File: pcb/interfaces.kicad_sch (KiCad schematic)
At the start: 6 parts

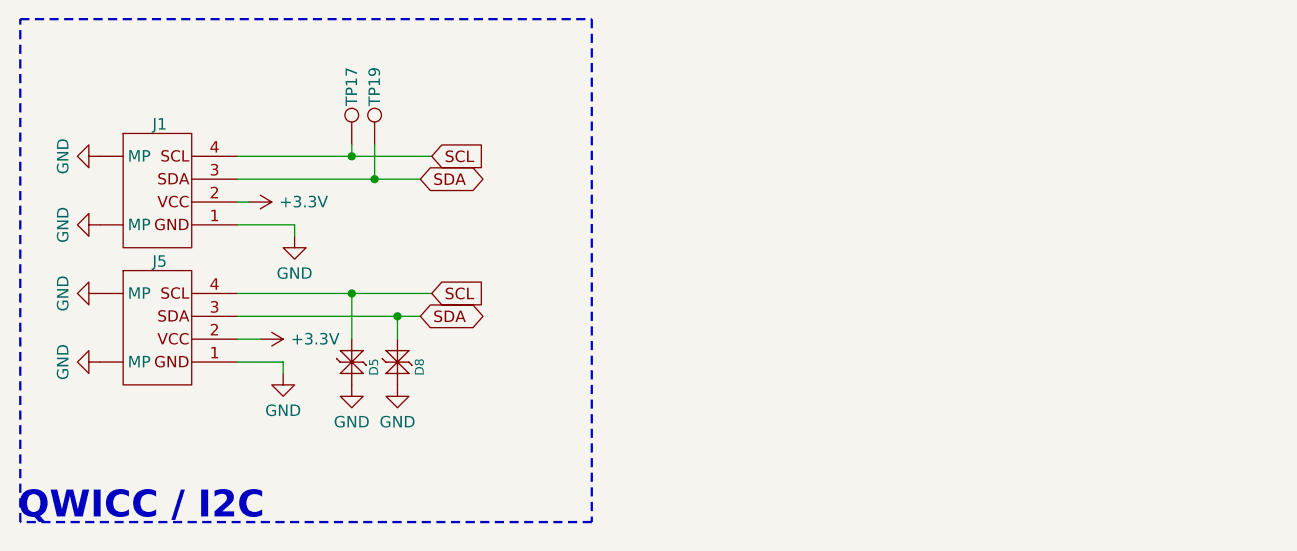
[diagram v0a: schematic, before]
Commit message: refactored to STM32
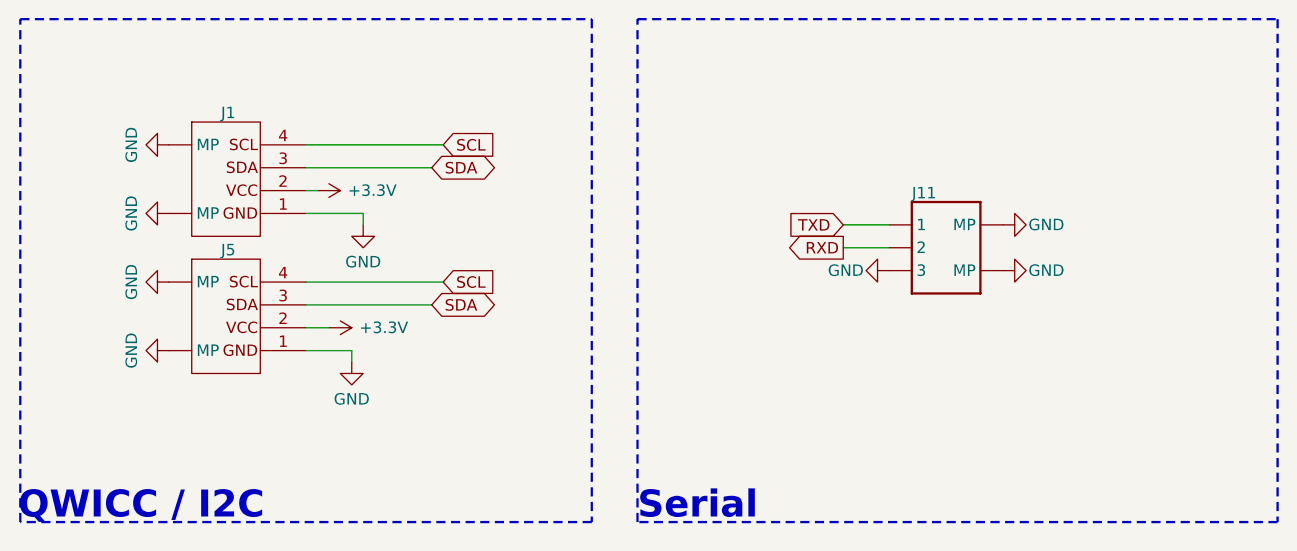
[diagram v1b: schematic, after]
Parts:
- removed D5, D8: PESD3V3S1BL, CRGM Passive:DFN1006-2, symbol CRGM Passive:PESD3V3S1BL
- removed TP17, TP19: ~, CRGM Mechanical:TestPoint_Pad_D1.0mm, symbol CRGM Connector:TestPoint
- added J11: (no value), CRGM Connector:JST_SH_BM03B-SRSS-TB_1x03-1MP_P1.00mm_Vertical, symbol CRGM Connector:JST-SH-3
- J1, J5: value ~ -> (none)
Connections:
- net GND: now also J11.0 (MP), J11.3, J11.4 (MP)
- new net RXD: J11.2
- new net TXD: J11.1
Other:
- note added: "Serial"
- moved on the sheet: J1, J5
